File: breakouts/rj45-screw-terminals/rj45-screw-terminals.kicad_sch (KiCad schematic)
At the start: 5 parts, among them J1 RJ45_LED_Shielded, J2 Conn_01x02, J3 TERM-BLK-8H-S

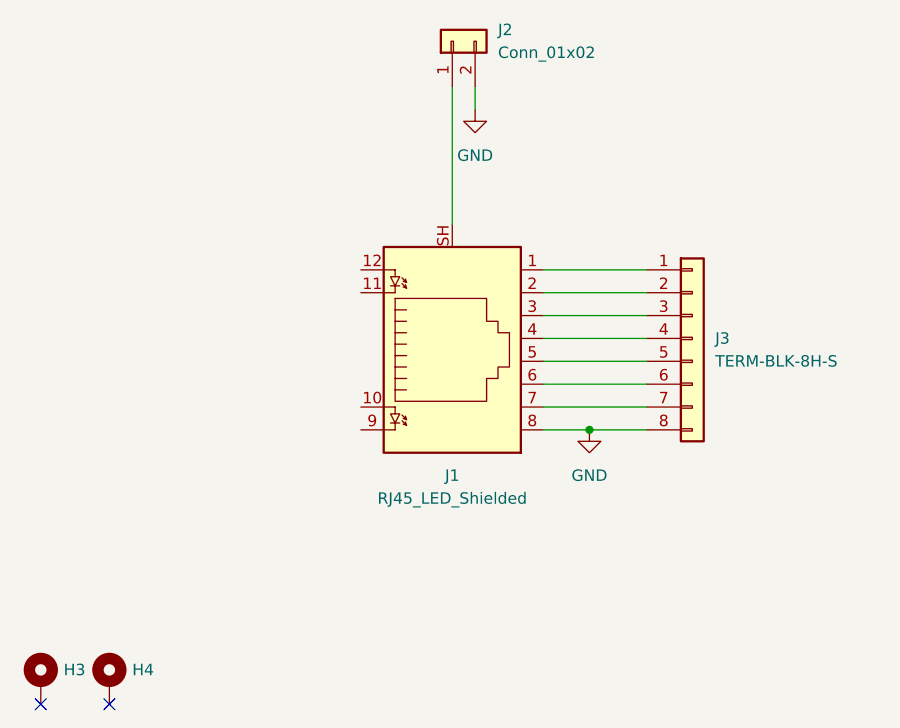
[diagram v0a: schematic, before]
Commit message: Fix ERC, add title information to sch, add initial version of build scripts
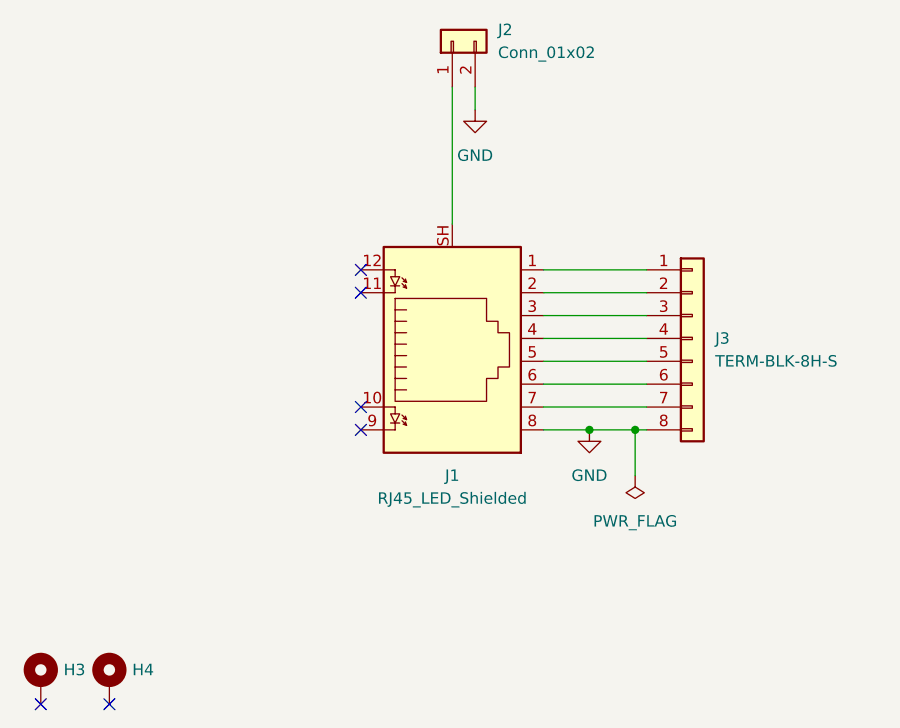
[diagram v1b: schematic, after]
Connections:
- no-connect marks 2 -> 6
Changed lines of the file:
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@@
 	(paper "A4")
+	(junction
+		(at 146.05 92.71)
+		(diameter 0)
+		(color 0 0 0 0)
+	)
 	(junction
 		(at 140.97 92.71)
@@
 	)
 	(no_connect
+		(at 115.57 74.93)
+	)
+	(no_connect
 		(at 80.01 123.19)
+	)
+	(no_connect
+		(at 115.57 92.71)
+	)
+	(no_connect
+		(at 115.57 90.17)
 	)
 	(no_connect
 		(at 87.63 123.19)
 	)
+	(no_connect
+		(at 115.57 77.47)
+	)
 	(wire
 		(pts
@@
 	(wire
 		(pts
+			(xy 146.05 92.71) (xy 147.32 92.71)
+		)
+		(stroke
+			(width 0)
+			(type default)
+		)
+	)
+	(wire
+		(pts
 			(xy 135.89 77.47) (xy 147.32 77.47)
 		)
@@
 	(wire
 		(pts
-			(xy 140.97 92.71) (xy 147.32 92.71)
+			(xy 140.97 92.71) (xy 146.05 92.71)
 		)
 		(stroke
@@
 		(pts
 			(xy 135.89 92.71) (xy 140.97 92.71)
+		)
+		(stroke
+			(width 0)
+			(type default)
+		)
+	)
+	(wire
+		(pts
+			(xy 146.05 92.71) (xy 146.05 97.79)
 		)
 		(stroke
@@
 					(unit 1)
 				)
+			)
+		)
+	)
+	(symbol
+		(lib_id "power:PWR_FLAG")
+		(at 146.05 97.79 180)
+		(unit 1)
+		(exclude_from_sim no)
+		(in_bom yes)
+		(on_board yes)
+		(dnp no)
+		(fields_autoplaced yes)
+		(property "Reference" "#FLG01"
+			(at 146.05 99.695 0)
+			(effects
+				(font
+					(size 1.27 1.27)
+				)
+				(hide yes)
+			)
+		)
+		(property "Value" "PWR_FLAG"
+			(at 146.05 102.87 0)
+			(effects
+				(font
+					(size 1.27 1.27)
+				)
+			)
+		)
+		(property "Footprint" ""
+			(at 146.05 97.79 0)
+			(effects
+				(font
+					(size 1.27 1.27)
+				)
+				(hide yes)
+			)
+		)
+		(property "Datasheet" "~"
+			(at 146.05 97.79 0)
+			(effects
+				(font
+					(size 1.27 1.27)
+				)
+				(hide yes)
+			)
+		)
+		(property "Description" "Special symbol for telling ERC where power comes from"
+			(at 146.05 97.79 0)
+			(effects
+				(font
+					(size 1.27 1.27)
+				)
+				(hide yes)
+			)
+		)
+		(pin "1"
+		)
+		(instances
+			(project ""
+				(path "/d87809ff-7d65-4cd2-aab6-9e40d92f859f"
+					(reference "#FLG01")
+					(unit 1)
+				)

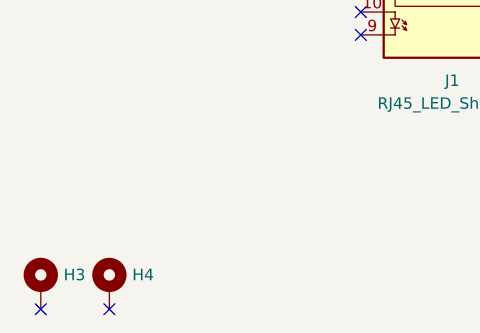
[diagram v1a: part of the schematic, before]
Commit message: Fill in BOM (LCSC#)
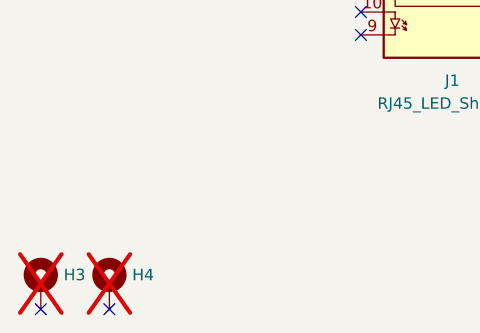
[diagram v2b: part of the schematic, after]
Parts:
- H3, H4: now not fitted
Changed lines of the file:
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@@
 		(in_bom no)
 		(on_board yes)
-		(dnp no)
+		(dnp yes)
 		(fields_autoplaced yes)
 		(property "Reference" "H3"
@@
 		(in_bom no)
 		(on_board yes)
-		(dnp no)
+		(dnp yes)
 		(fields_autoplaced yes)
 		(property "Reference" "H4"
